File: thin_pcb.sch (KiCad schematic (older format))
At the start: 149 parts, among them J01 Conn_01x02, J02 Conn_01x02, J04 Conn_01x02, J06 Conn_01x02, J07 Conn_01x02, J08 Conn_01x02, J1 USB_B_Micro, J11 Conn_01x03, J12 Conn_01x03, J13 Conn_01x03, J14 Conn_01x03, J15 Conn_01x03, J16 Conn_01x03, J17 Conn_01x03, J18 Conn_01x03, J2 AudioJack4_Ground, J21 Conn_01x07, J22 Conn_01x07, J23 Conn_01x07, J24 Conn_01x07, J25 Conn_01x07, J26 Conn_01x07, J27 Conn_01x07, J28 Conn_01x07, J3 AudioJack4_Ground, J31 Conn_01x07, J32 Conn_01x07, J33 Conn_01x07, J34 Conn_01x07, J35 Conn_01x07, J36 Conn_01x07, J37 Conn_01x07, J38 Conn_01x07, J4 Conn_01x06, J41 Conn_01x04, J42 Conn_01x04, J43 Conn_01x04, J44 Conn_01x04, J45 Conn_01x04, J46 Conn_01x04, J47 Conn_01x04, J48 Conn_01x04, J5 Conn_01x06, J51 Conn_01x01, J52 Conn_01x01, J53 Conn_01x01, J54 Conn_01x01, J55 Conn_01x01, J56 Conn_01x01, J57 Conn_01x01, J58 Conn_01x01, J6 Conn_02x02, J7 Conn_01x02, SW11 SW_Push, SW12 SW_Push, SW13 SW_Push, SW14 SW_Push, SW15 SW_Push, SW21 SW_Push, SW22 SW_Push, SW23 SW_Push, SW24 SW_Push, SW25 SW_Push, SW252 SW_Push, SW31 SW_Push, SW32 SW_Push, SW33 SW_Push, SW34 SW_Push, SW35 SW_Push, SW41 SW_Push, SW42 SW_Push, SW422 SW_Push, SW43 SW_Push, SW44 SW_Push, SW45 SW_Push, SW452 SW_Push, SW51 SW_Push, SW52 SW_Push, SW522 SW_Push, SW53 SW_Push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

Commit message: hide unwanted labels
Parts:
- J01, J02, J04, J06, J07, J08, J7: footprint Connector_PinSocket_2.54mm:PinSocket_1x02_P2.54mm_Vertical -> lib:PinSocket_1x02_P2.54mm_Vertical
- J11, J12, J13, J14, J15, J16, J17, J18: footprint Connector_PinSocket_2.54mm:PinSocket_1x03_P2.54mm_Vertical -> lib:PinSocket_1x03_P2.54mm_Vertical
- J21, J22, J23, J24, J25, J26, J27, J28, J31, J32, J33, J34, J35, J36, J37, J38, J41, J42, J43, J44, J45, J46, J47, J48: footprint Connector_PinSocket_2.54mm:PinSocket_1x07_P2.54mm_Vertical -> lib:PinSocket_1x07_P2.54mm_Vertical
- J4, J5: footprint Connector_PinSocket_2.54mm:PinSocket_1x06_P2.54mm_Vertical -> lib:PinSocket_1x06_P2.54mm_Vertical
- J51, J52, J53, J54, J55, J56, J57, J58: footprint Connector_PinSocket_2.54mm:PinSocket_1x01_P2.54mm_Vertical -> lib:PinSocket_1x01_P2.54mm_Vertical
- J6: footprint Connector_PinSocket_2.54mm:PinSocket_2x02_P2.54mm_Vertical -> lib:PinSocket_2x02_P2.54mm_Vertical

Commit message: smd 0603->1005 & fixes
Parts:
- removed C1, C2: 22p, Capacitor_SMD:C_0201_0603Metric, symbol Device:C_Small
- C3, C4, C5, C6, C7: footprint Capacitor_SMD:C_0201_0603Metric -> Capacitor_SMD:C_0402_1005Metric
- F1: footprint Fuse:Fuse_0402_1005Metric -> Fuse:Fuse_0603_1608Metric
- R1, R4, R5, R6: footprint Resistor_SMD:R_0201_0603Metric -> Resistor_SMD:R_0402_1005Metric
- Y1: footprint Crystal:Crystal_SMD_2012-2Pin_2.0x1.2mm -> Crystal:Resonator_SMD_muRata_CSTxExxV-3Pin_3.0x1.1mm; symbol Device:Crystal -> Device:Crystal_GND2
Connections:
- net GND: now also Y1.2
- net UD+: no longer J7.1 (Pin_1), R2.2, U2.4 (IO2)
- net UD-: no longer J7.2 (Pin_2), R3.1, U2.6 (IO1)
- net XTAL2: now also Y1.3; no longer Y1.2
- new net CD+: J7.1 (Pin_1), R2.2, U2.4 (IO2)
- new net CD-: J7.2 (Pin_2), R3.1, U2.6 (IO1)
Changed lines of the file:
@@
 Text GLabel 1000 5100 0    50   Input ~ 0
 D+
-$Comp
-L Device:C_Small C1
-U 1 1 5CFBF258
-P 3400 6900
-F 0 "C1" H 3308 6946 50  0000 R CNN
-F 1 "22p" H 3308 6855 50  0000 R CNN
-F 2 "Capacitor_SMD:C_0201_0603Metric" H 3400 6900 50  0001 C CNN
-F 3 "~" H 3400 6900 50  0001 C CNN
-	1    3400 6900
-	1    0    0    -1
-$EndComp
-Text GLabel 3400 6550 1    50   Input ~ 0
+Text GLabel 3550 6750 0    50   Input ~ 0
 XTAL1
-Text GLabel 4000 6550 1    50   Input ~ 0
+Text GLabel 3850 6750 2    50   Input ~ 0
 XTAL2
-Wire Wire Line
-	3400 6550 3400 6750
-Wire Wire Line
-	3550 6750 3400 6750
-$Comp
-L power:GND #PWR05
-U 1 1 5CFBFEAA
-P 4000 7000
-F 0 "#PWR05" H 4000 6750 50  0001 C CNN
-F 1 "GND" H 4005 6827 50  0000 C CNN
-F 2 "" H 4000 7000 50  0001 C CNN
-F 3 "" H 4000 7000 50  0001 C CNN
-	1    4000 7000
-	1    0    0    -1
-$EndComp
-$Comp
-L Device:C_Small C2
-U 1 1 5CFC06D4
-P 4000 6900
-F 0 "C2" H 4092 6946 50  0000 L CNN
-F 1 "22p" H 4092 6855 50  0000 L CNN
-F 2 "Capacitor_SMD:C_0201_0603Metric" H 4000 6900 50  0001 C CNN
-F 3 "~" H 4000 6900 50  0001 C CNN
-	1    4000 6900
-	1    0    0    -1
-$EndComp
-Wire Wire Line
-	3400 6800 3400 6750
-Connection ~ 3400 6750
-Wire Wire Line
-	4000 6550 4000 6750
-Wire Wire Line
-	3850 6750 4000 6750
-Wire Wire Line
-	4000 6800 4000 6750
-Connection ~ 4000 6750
 Text GLabel 1000 4300 0    50   Input ~ 0
 XTAL1
@@
 F 0 "R1" V 6850 5300 50  0000 L CNN
 F 1 "10k" V 6950 5300 50  0000 L CNN
-F 2 "Resistor_SMD:R_0201_0603Metric" V 6880 5350 50  0001 C CNN
+F 2 "Resistor_SMD:R_0402_1005Metric" V 6880 5350 50  0001 C CNN
 F 3 "~" H 6950 5350 50  0001 C CNN
 	1    6950 5350
@@
 F 0 "C3" V 1010 5400 50  0000 C CNN
 F 1 "1u" V 1101 5400 50  0000 C CNN
-F 2 "Capacitor_SMD:C_0201_0603Metric" H 888 5250 50  0001 C CNN
+F 2 "Capacitor_SMD:C_0402_1005Metric" H 888 5250 50  0001 C CNN
 F 3 "~" H 850 5400 50  0001 C CNN
 	1    850  5400
@@
 F 0 "C4" H 2885 5654 50  0000 R CNN
 F 1 "0.1u" H 2885 5745 50  0000 R CNN
-F 2 "Capacitor_SMD:C_0201_0603Metric" H 3038 5550 50  0001 C CNN
+F 2 "Capacitor_SMD:C_0402_1005Metric" H 3038 5550 50  0001 C CNN
 F 3 "~" H 3000 5700 50  0001 C CNN
 	1    3000 5700
@@
 F 0 "C5" H 3285 5654 50  0000 R CNN
 F 1 "0.1u" H 3285 5745 50  0000 R CNN
-F 2 "Capacitor_SMD:C_0201_0603Metric" H 3438 5550 50  0001 C CNN
+F 2 "Capacitor_SMD:C_0402_1005Metric" H 3438 5550 50  0001 C CNN
 F 3 "~" H 3400 5700 50  0001 C CNN
 	1    3400 5700
@@
 F 0 "C6" H 3685 5654 50  0000 R CNN
 F 1 "0.1u" H 3685 5745 50  0000 R CNN
-F 2 "Capacitor_SMD:C_0201_0603Metric" H 3838 5550 50  0001 C CNN
+F 2 "Capacitor_SMD:C_0402_1005Metric" H 3838 5550 50  0001 C CNN
 F 3 "~" H 3800 5700 50  0001 C CNN
 	1    3800 5700
@@
 F 0 "C7" H 4085 5654 50  0000 R CNN
 F 1 "0.1u" H 4085 5745 50  0000 R CNN
-F 2 "Capacitor_SMD:C_0201_0603Metric" H 4238 5550 50  0001 C CNN
+F 2 "Capacitor_SMD:C_0402_1005Metric" H 4238 5550 50  0001 C CNN
 F 3 "~" H 4200 5700 50  0001 C CNN
 	1    4200 5700
@@
 F 0 "R4" V 7700 5850 50  0000 L CNN
 F 1 "10k" V 7800 5850 50  0000 L CNN
-F 2 "Resistor_SMD:R_0201_0603Metric" V 7730 5900 50  0001 C CNN
+F 2 "Resistor_SMD:R_0402_1005Metric" V 7730 5900 50  0001 C CNN
 F 3 "~" H 7800 5900 50  0001 C CNN
 	1    7800 5900
@@
 F 0 "R5" V 8000 5850 50  0000 L CNN
 F 1 "10k" V 8100 5850 50  0000 L CNN
-F 2 "Resistor_SMD:R_0201_0603Metric" V 8030 5900 50  0001 C CNN
+F 2 "Resistor_SMD:R_0402_1005Metric" V 8030 5900 50  0001 C CNN
 F 3 "~" H 8100 5900 50  0001 C CNN
 	1    8100 5900
@@
 F 0 "F1" V 5850 5200 50  0000 C CNN
 F 1 "500m" V 5950 5200 50  0000 C CNN
-F 2 "Fuse:Fuse_0402_1005Metric" H 6100 5000 50  0001 L CNN
+F 2 "Fuse:Fuse_0603_1608Metric" H 6100 5000 50  0001 L CNN
 F 3 "~" H 6050 5200 50  0001 C CNN
 	1    6050 5200
@@
 F 0 "R6" V 2250 6200 50  0000 C CNN
 F 1 "10k" V 2350 6200 50  0000 C CNN
-F 2 "Resistor_SMD:R_0201_0603Metric" V 2280 6200 50  0001 C CNN
+F 2 "Resistor_SMD:R_0402_1005Metric" V 2280 6200 50  0001 C CNN
 F 3 "~" H 2350 6200 50  0001 C CNN
 	1    2350 6200
@@
 $EndComp
 $Comp
-L power:GND #PWR0133
-U 1 1 5CF9CD82
-P 3400 7000
-F 0 "#PWR0133" H 3400 6750 50  0001 C CNN
-F 1 "GND" H 3405 6827 50  0000 C CNN
-F 2 "" H 3400 7000 50  0001 C CNN
-F 3 "" H 3400 7000 50  0001 C CNN
-	1    3400 7000
-	1    0    0    -1
-$EndComp
-$Comp
 L power:VCC #PWR0126
 U 1 1 5CFAAF32
@@
 $EndComp
 Text GLabel 4500 7400 0    50   Input ~ 0
-UD+
+CD+
 Text GLabel 4500 7500 0    50   Input ~ 0
-UD-
-$Comp
-L Device:Crystal Y1
+CD-
+$Comp
+L Device:Crystal_GND2 Y1
 U 1 1 5CFA75EF
 P 3700 6750
 F 0 "Y1" H 3700 7018 50  0000 C CNN
 F 1 "Crystal" H 3700 6927 50  0000 C CNN
-F 2 "Crystal:Crystal_SMD_2012-2Pin_2.0x1.2mm" H 3700 6750 50  0001 C CNN
+F 2 "Crystal:Resonator_SMD_muRata_CSTxExxV-3Pin_3.0x1.1mm" H 3700 6750 50  0001 C CNN
 F 3 "~" H 3700 6750 50  0001 C CNN
 	1    3700 6750
@@
 	1    0    0    -1
 $EndComp
-Wire Wire Line
-	6100 7050 6100 6850
-Connection ~ 6100 6850
-Wire Wire Line
-	5100 7050 5100 6850
-Connection ~ 5100 6850
 Connection ~ 900  1300
 Connection ~ 1200 900
@@
 Wire Wire Line
 	7400 3150 6900 3150
+$Comp
+L power:GND #PWR0117
+U 1 1 5D2FEF38
+P 3700 6950
+F 0 "#PWR0117" H 3700 6700 50  0001 C CNN
+F 1 "GND" H 3705 6777 50  0000 C CNN
+F 2 "" H 3700 6950 50  0001 C CNN
+F 3 "" H 3700 6950 50  0001 C CNN
+	1    3700 6950
+	1    0    0    -1
+$EndComp
+Text GLabel 6400 6950 2    50   Input ~ 0
+CD+
+Text GLabel 4800 6950 0    50   Input ~ 0
+CD-
+Wire Wire Line
+	6100 6850 6100 6950
+Wire Wire Line
+	6100 6950 6400 6950
+Connection ~ 6100 6850
+Wire Wire Line
+	5100 6850 5100 6950
+Wire Wire Line
+	5100 6950 4800 6950
+Connection ~ 5100 6850
 $EndSCHEMATC

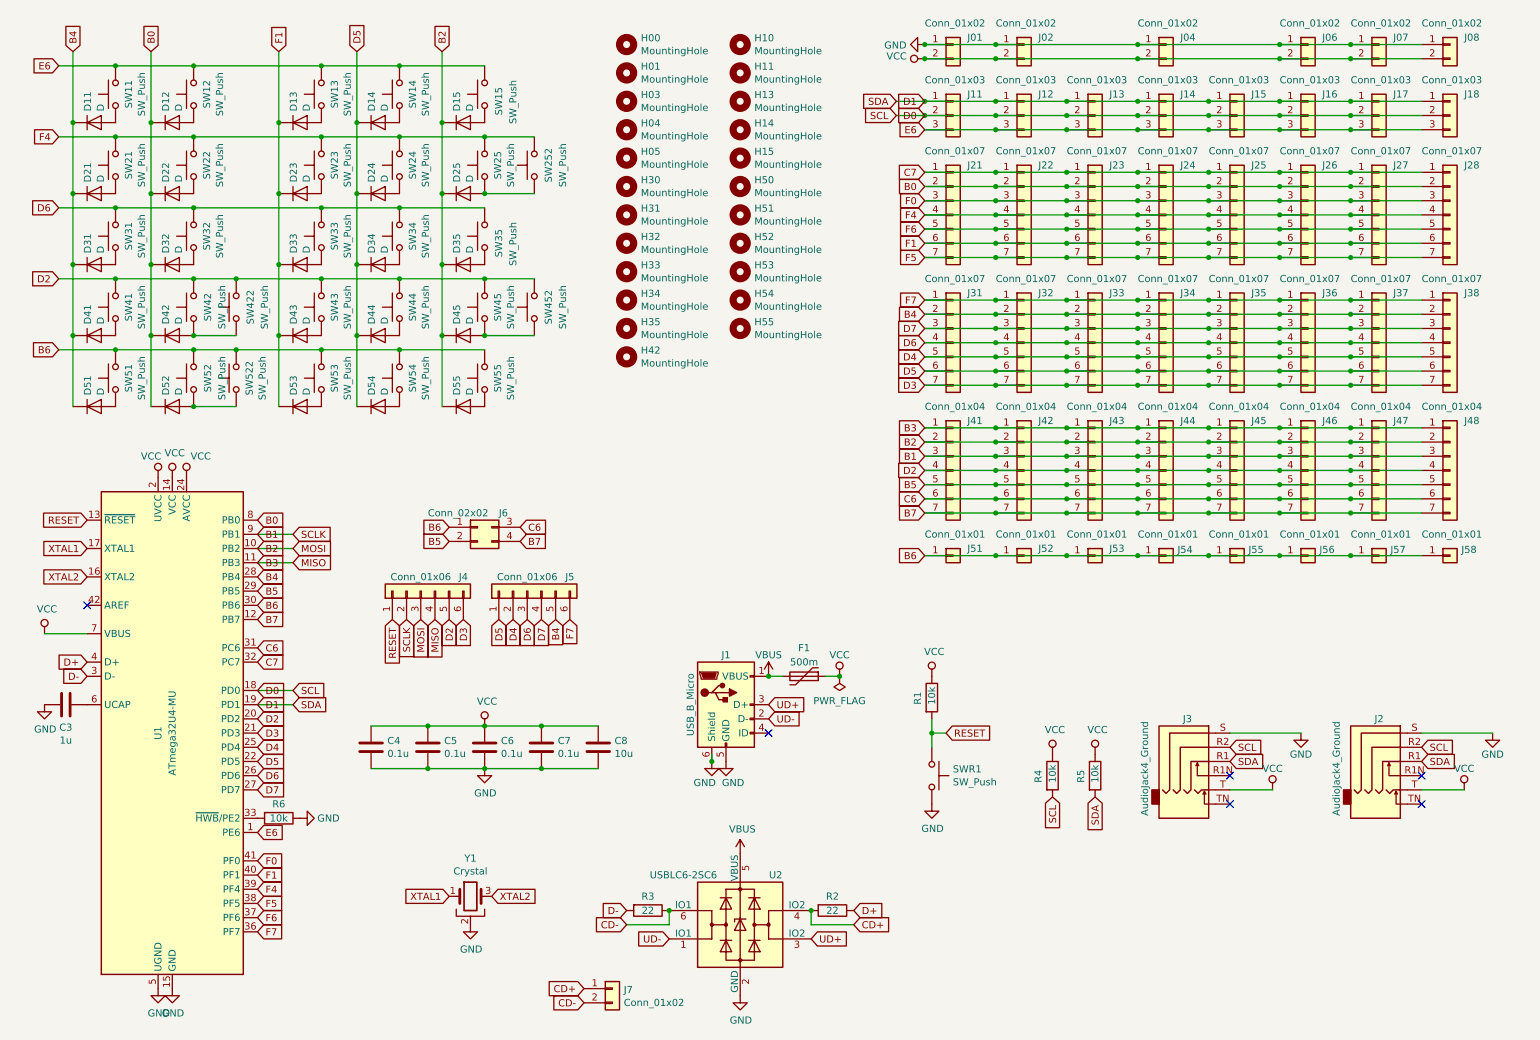
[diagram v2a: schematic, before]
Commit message: aref cond & positioning
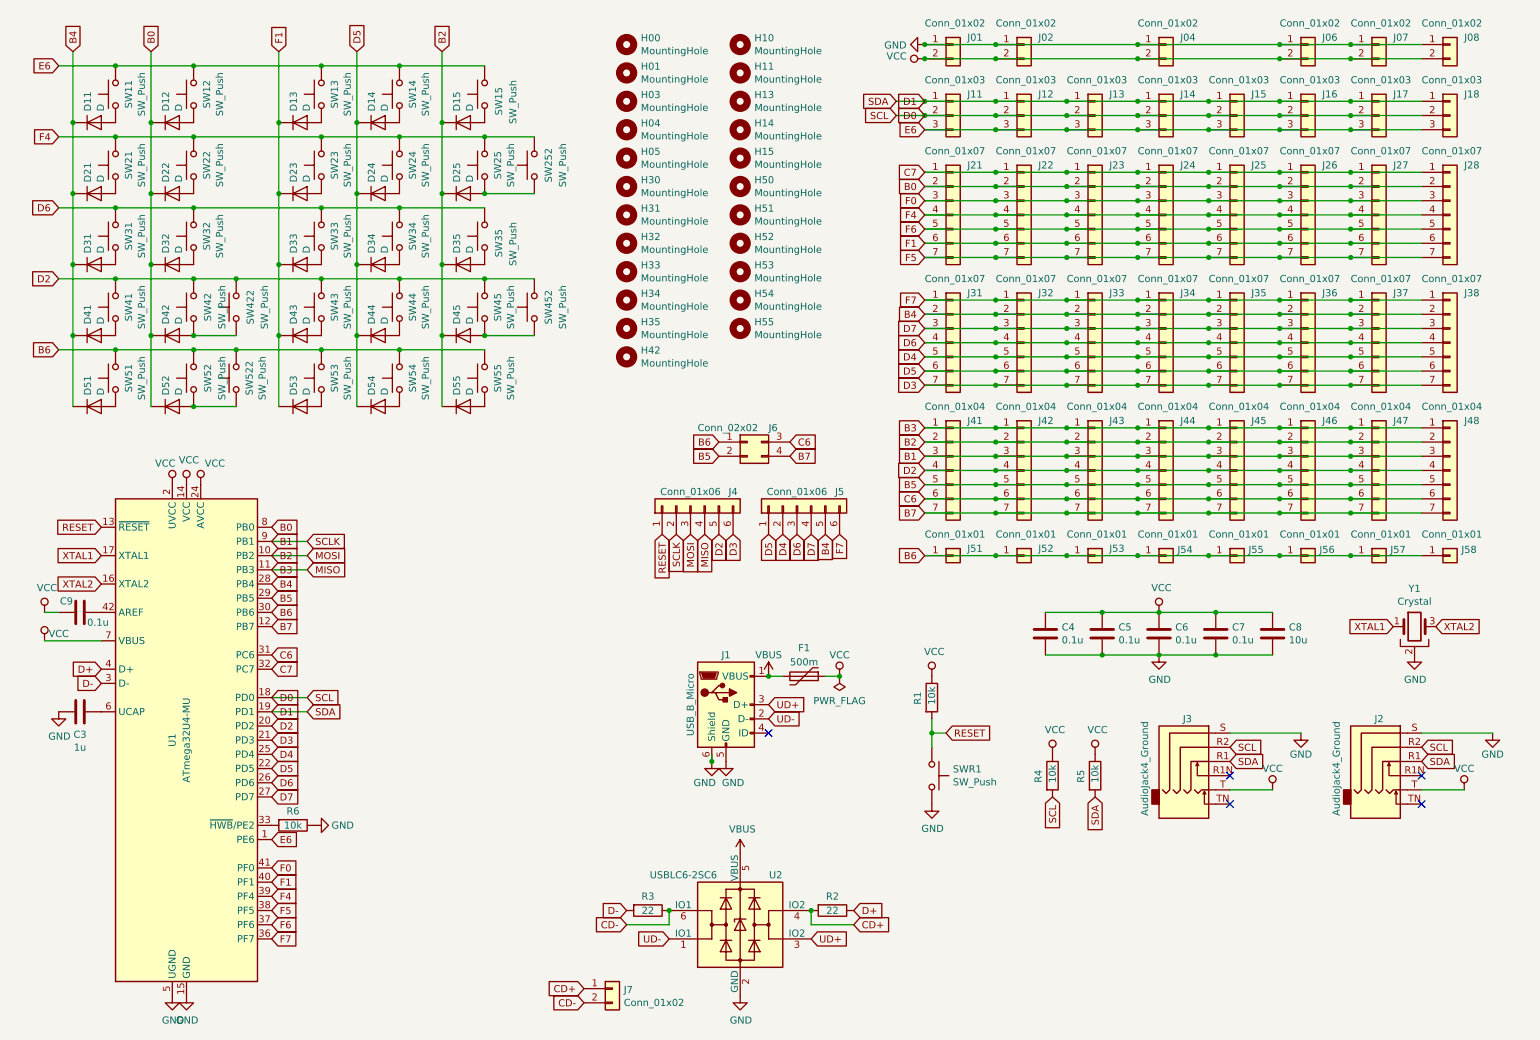
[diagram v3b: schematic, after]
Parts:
- added C9: 0.1u, Capacitor_SMD:C_0402_1005Metric, symbol Device:C
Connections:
- net VCC: now also C9.1
- net at U1.42 (AREF): now also C9.2
- no-connect marks 6 -> 5
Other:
- moved on the sheet: C3, C4, C5, C6, C7, C8, J4, J5, J6, R6, U1, Y1

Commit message: reset switch & aligning
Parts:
- SWR1: footprint Button_Switch_SMD:SW_SPST_EVQP7C -> lib:SW_Reset
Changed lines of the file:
@@
 F 0 "SWR1" V 6904 6048 50  0000 L CNN
 F 1 "SW_Push" V 6995 6048 50  0000 L CNN
-F 2 "Button_Switch_SMD:SW_SPST_EVQP7C" H 6950 6100 50  0001 C CNN
+F 2 "lib:SW_Reset" H 6950 6100 50  0001 C CNN
 F 3 "" H 6950 6100 50  0001 C CNN
 	1    6950 5900

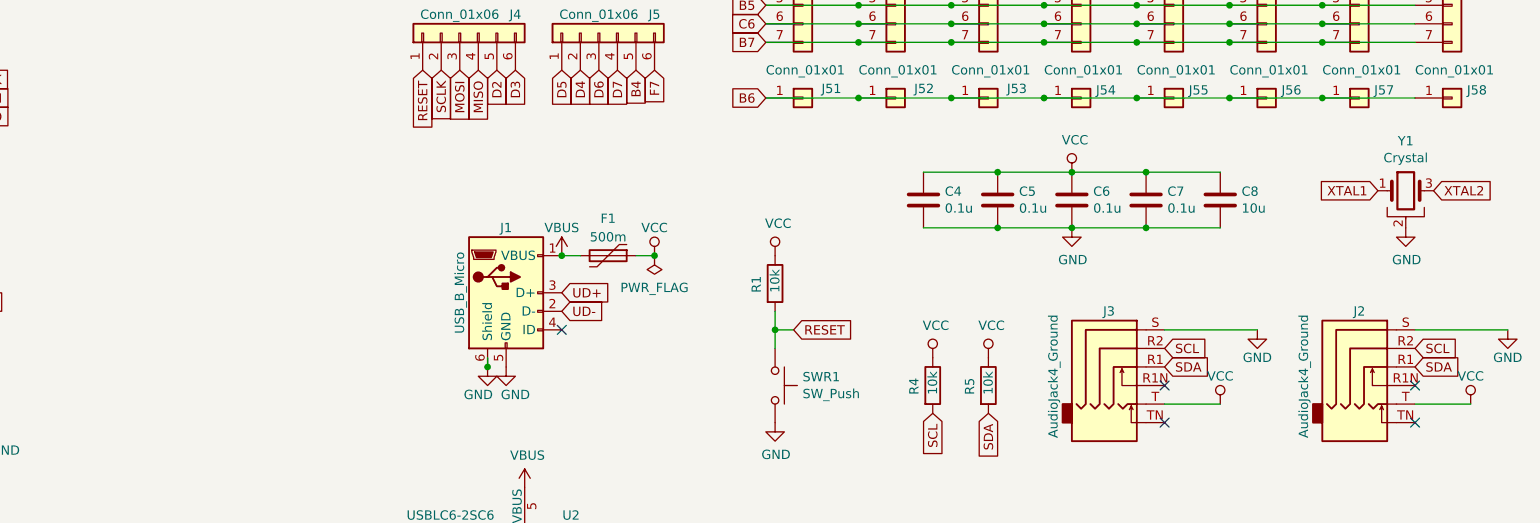
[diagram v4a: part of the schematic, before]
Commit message: pcb class 0.2
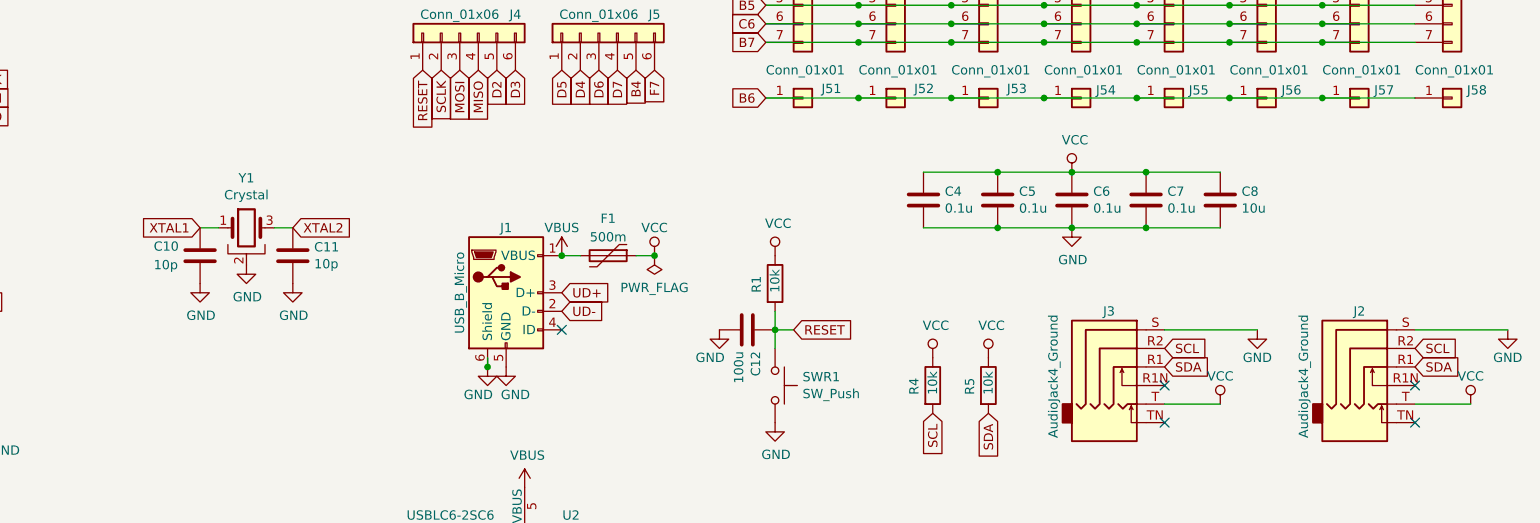
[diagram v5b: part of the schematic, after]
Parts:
- added C10, C11: 10p, Capacitor_SMD:C_0402_1005Metric, symbol Device:C
- added C12: 100u, Capacitor_SMD:C_0402_1005Metric, symbol Device:C
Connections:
- net GND: now also C10.1, C11.1, C12.1
- net RESET: now also C12.2
- net XTAL1: now also C10.2
- net XTAL2: now also C11.2
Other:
- moved on the sheet: Y1
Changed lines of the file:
@@
 Text GLabel 1100 5150 0    50   Input ~ 0
 D+
-Text GLabel 10200 4850 0    50   Input ~ 0
+Text GLabel 3850 5050 0    50   Input ~ 0
 XTAL1
-Text GLabel 10500 4850 2    50   Input ~ 0
+Text GLabel 4350 5050 2    50   Input ~ 0
 XTAL2
 Text GLabel 1100 4350 0    50   Input ~ 0
@@
 L Device:Crystal_GND2 Y1
 U 1 1 5CFA75EF
-P 10350 4850
-F 0 "Y1" H 10350 5118 50  0000 C CNN
-F 1 "Crystal" H 10350 5027 50  0000 C CNN
-F 2 "Crystal:Resonator_SMD_muRata_CSTxExxV-3Pin_3.0x1.1mm" H 10350 4850 50  0001 C CNN
-F 3 "~" H 10350 4850 50  0001 C CNN
-	1    10350 4850
+P 4100 5050
+F 0 "Y1" H 4100 5318 50  0000 C CNN
+F 1 "Crystal" H 4100 5227 50  0000 C CNN
+F 2 "Crystal:Resonator_SMD_muRata_CSTxExxV-3Pin_3.0x1.1mm" H 4100 5050 50  0001 C CNN
+F 3 "~" H 4100 5050 50  0001 C CNN
+	1    4100 5050
 	1    0    0    -1
 $EndComp
@@
 L power:GND #PWR0117
 U 1 1 5D2FEF38
-P 10350 5050
-F 0 "#PWR0117" H 10350 4800 50  0001 C CNN
-F 1 "GND" H 10355 4877 50  0000 C CNN
-F 2 "" H 10350 5050 50  0001 C CNN
-F 3 "" H 10350 5050 50  0001 C CNN
-	1    10350 5050
+P 4100 5250
+F 0 "#PWR0117" H 4100 5000 50  0001 C CNN
+F 1 "GND" H 4105 5077 50  0000 C CNN
+F 2 "" H 4100 5250 50  0001 C CNN
+F 3 "" H 4100 5250 50  0001 C CNN
+	1    4100 5250
 	1    0    0    -1
 $EndComp
@@
 $EndComp
 $Comp
-L power:VCC #PWR?
+L power:VCC #PWR0122
 U 1 1 5D381969
 P 700 4750
-F 0 "#PWR?" H 700 4600 50  0001 C CNN
+F 0 "#PWR0122" H 700 4600 50  0001 C CNN
 F 1 "VCC" H 717 4923 50  0000 C CNN
 F 2 "" H 700 4750 50  0001 C CNN
@@
 Wire Wire Line
 	700  4950 1100 4950
+$Comp
+L Device:C C11
+U 1 1 5D3C4437
+P 4350 5200
+F 0 "C11" H 4235 5154 50  0000 R CNN
+F 1 "10p" H 4235 5245 50  0000 R CNN
+F 2 "Capacitor_SMD:C_0402_1005Metric" H 4388 5050 50  0001 C CNN
+F 3 "~" H 4350 5200 50  0001 C CNN
+	1    4350 5200
+	-1   0    0    1
+$EndComp
+$Comp
+L Device:C C10
+U 1 1 5D3C45A7
+P 3850 5200
+F 0 "C10" H 4100 5150 50  0000 R CNN
+F 1 "10p" H 4100 5250 50  0000 R CNN
+F 2 "Capacitor_SMD:C_0402_1005Metric" H 3888 5050 50  0001 C CNN
+F 3 "~" H 3850 5200 50  0001 C CNN
+	1    3850 5200
+	-1   0    0    1
+$EndComp
+Wire Wire Line
+	3850 5050 3950 5050
+Wire Wire Line
+	4350 5050 4250 5050
+$Comp
+L power:GND #PWR0129
+U 1 1 5D442F97
+P 3850 5350
+F 0 "#PWR0129" H 3850 5100 50  0001 C CNN
+F 1 "GND" H 3855 5177 50  0000 C CNN
+F 2 "" H 3850 5350 50  0001 C CNN
+F 3 "" H 3850 5350 50  0001 C CNN
+	1    3850 5350
+	1    0    0    -1
+$EndComp
+$Comp
+L power:GND #PWR0130
+U 1 1 5D4430CE
+P 4350 5350
+F 0 "#PWR0130" H 4350 5100 50  0001 C CNN
+F 1 "GND" H 4355 5177 50  0000 C CNN
+F 2 "" H 4350 5350 50  0001 C CNN
+F 3 "" H 4350 5350 50  0001 C CNN
+	1    4350 5350
+	1    0    0    -1
+$EndComp
+$Comp
+L Device:C C12
+U 1 1 5D41E222
+P 6800 5600
+F 0 "C12" H 6685 5554 50  0000 R CNN
+F 1 "100u" H 6685 5645 50  0000 R CNN
+F 2 "Capacitor_SMD:C_0402_1005Metric" H 6838 5450 50  0001 C CNN
+F 3 "~" H 6800 5600 50  0001 C CNN
+	1    6800 5600
+	0    -1   -1   0
+$EndComp
+$Comp
+L power:GND #PWR?
+U 1 1 5D41E725
+P 6650 5600
+F 0 "#PWR?" H 6650 5350 50  0001 C CNN
+F 1 "GND" H 6600 5450 50  0000 C CNN
+F 2 "" H 6650 5600 50  0001 C CNN
+F 3 "" H 6650 5600 50  0001 C CNN
+	1    6650 5600
+	1    0    0    -1
+$EndComp
 $EndSCHEMATC
